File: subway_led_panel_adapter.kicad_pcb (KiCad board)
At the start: 4 copper layers, 63.5 x 63.5 mm, 28 parts, among them J1 Conn_02x06_Odd_Even, J2 Conn_02x10_Odd_Even, J3 Conn_02x06_Odd_Even, J4 Conn_02x20_Odd_Even, U1 74AHCT244, U2 ChinaBluePill, U3 74LVC1G123

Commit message: more work
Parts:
- added H1: MountingHole_Pad, MountingHole:MountingHole_3.2mm_M3_Pad, F.Cu at (124.5, 104.1)
- added H2: MountingHole_Pad, MountingHole:MountingHole_3.2mm_M3_Pad, F.Cu at (176.5, 48.3)
- added R9: 1k, Resistor_SMD:R_0603_1608Metric, F.Cu at (158.2, 86.2)
- R3: value 1k -> 100k
- moved J3 0.76 mm to (150.9, 61.0)
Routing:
- net /PB15: track 25.7 -> 40.2 mm, vias 0 -> 1
- net /PB14: track 30.0 -> 43.3 mm, vias 1 -> 0
- net /ROW_~{E1}: track 91.4 -> 80.2 mm, vias 2 -> 3
- net /~{OE}/SW/~{ED}_inv_LV: track 64.1 -> 56.9 mm, vias 2 -> 1
- net /LE/MOD/CA_LV: track 28.8 -> 35.9 mm
- net /PA9: track 39.7 -> 46.6 mm
- net /PB3: track 43.2 -> 47.3 mm
- net /ROW_A2: track 13.9 -> 11.2 mm, vias 0 -> 1
- net +3V3: track 88.9 -> 86.4 mm, vias 0 -> 1
- net /PB1: track 10.5 -> 12.8 mm
- net /PB4: track 49.8 -> 52.1 mm
- net /COPI_LV: track 35.4 -> 33.2 mm, vias 2 -> 1
- net /PB11: track 10.8 -> 8.64 mm
- net GND: track 18.8 -> 21.0 mm
- net /PB12: track 33.3 -> 35.2 mm
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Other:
- board size 63.5 x 63.5 mm -> 59.7 x 63.5 mm
- board text added: "Default Shiftregister Chain: COPI - Reg A - ... ... - Reg C - Reg B - CIPO"
- board text removed: "Default Shiftregister Chain: COPI - Reg A - Reg C - Reg B - CIPO"

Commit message: general cleanup
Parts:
- moved D4 2.69 mm to (166.4, 47.0)
- moved R8 2.69 mm to (166.4, 50.9)
- moved D1 2.54 mm to (164.0, 47.0)
- moved R5 2.54 mm to (164.0, 50.9)
- moved D2 2.43 mm to (161.5, 47.0)
- moved R6 2.43 mm to (161.5, 50.9)
- moved C1 2.17 mm to (157.2, 91.1)
- moved D3 2.14 mm to (168.7, 47.0)
- moved R7 2.14 mm to (168.7, 50.9)
- moved R1 1.78 mm to (166.9, 64.8)
- moved R2 1.78 mm to (166.9, 66.5)
- moved R9 1.14 mm to (157.2, 86.7), turned to -90 degrees
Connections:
- J1 pad 10: GND -> /PA15
- J3 pad 10: GND -> /PA10
- U2 pad PA10: (no net) -> /PA10
- U2 pad PA15: (no net) -> /PA15
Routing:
- net /PA15: track 0.00 -> 58.0 mm
- net /PA10: track 0.00 -> 51.8 mm
- net /ROW_E2: track 80.6 -> 83.5 mm
- net /CIPO_5V: track 5.01 -> 2.57 mm
- net +5V: track 19.0 -> 16.9 mm
- net /ROW_~{E1}: track 80.2 -> 78.2 mm
- net GND: track 21.0 -> 19.1 mm
- net /LE/MOD/CA_LV: track 35.9 -> 34.9 mm
- net /PB12: track 35.2 -> 34.3 mm
- net /PB13: track 33.4 -> 32.5 mm
- net /PB14: track 43.3 -> 42.6 mm
- net /PB15: track 40.2 -> 39.6 mm
- net /PB10: track 13.7 -> 13.1 mm
- net /PB1: track 12.8 -> 12.3 mm, vias 0 -> 1
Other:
- board text added: "3v3 5V E2 ~{E1}"
- board text removed: "5V 3v3 ~{E1} E2"

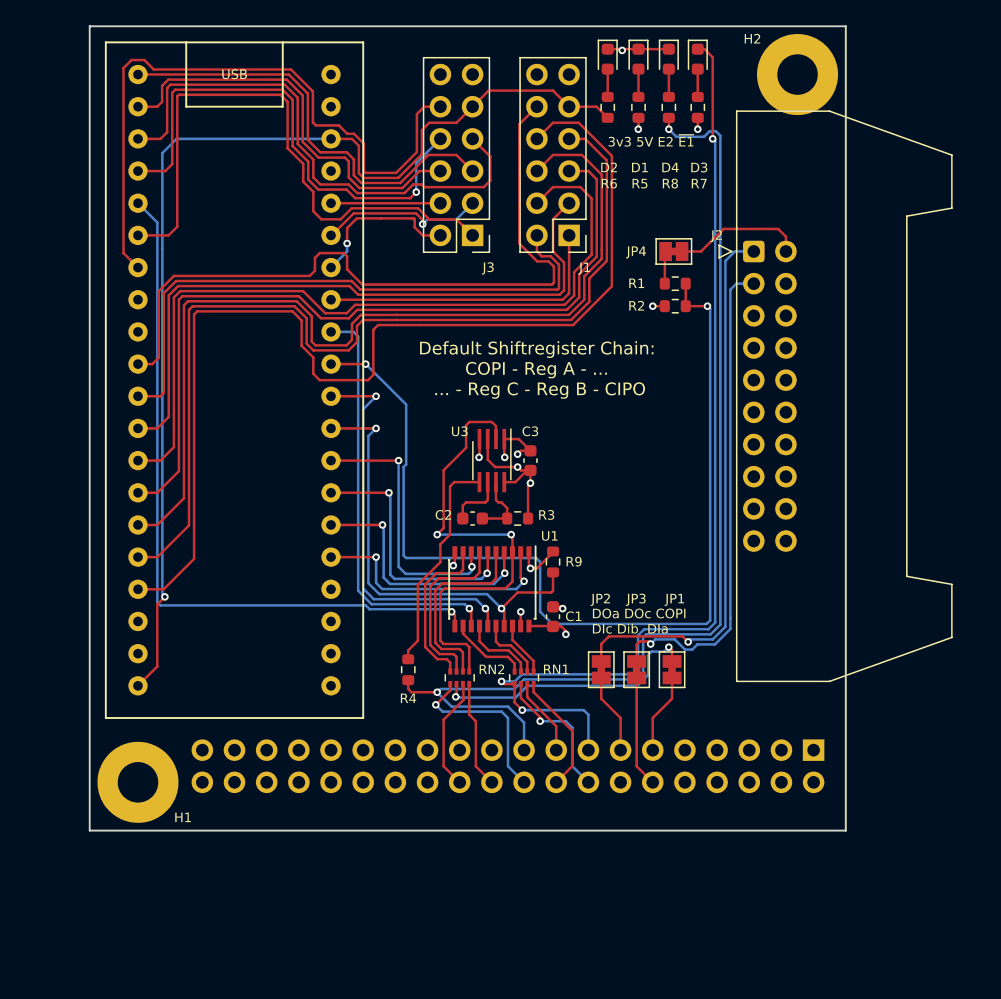
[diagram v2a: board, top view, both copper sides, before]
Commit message: Add "pmpd" style connector for 3v3 signals, rearrange, add mounting holes.
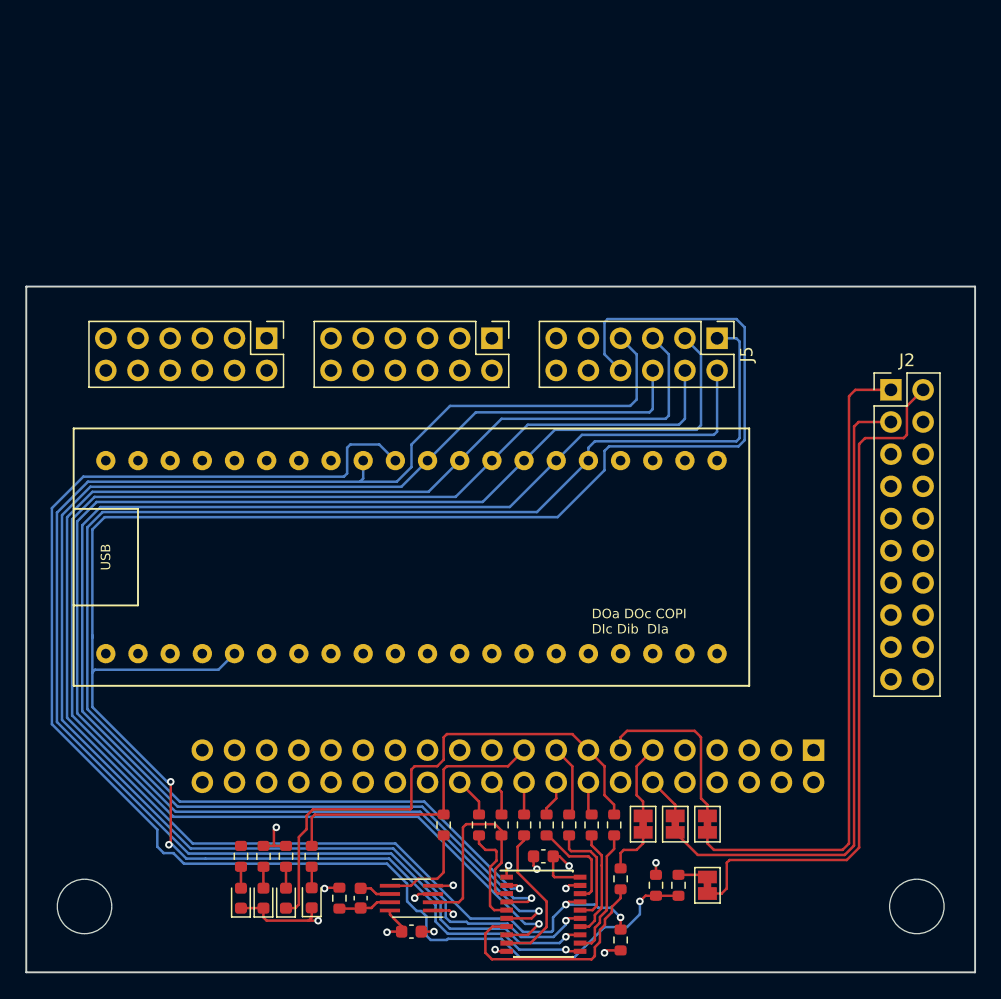
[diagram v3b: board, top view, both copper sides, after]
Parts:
- removed H1, H2: MountingHole_Pad, MountingHole:MountingHole_3.2mm_M3_Pad
- removed RN1, RN2: 68R, Resistor_SMD:R_Array_Concave_4x0402
- added H3: MountingHole, MountingHole:MountingHole_4.3mm_M4, F.Cu at (120.2, 113.9)
- added H4: MountingHole, MountingHole:MountingHole_4.3mm_M4, F.Cu at (185.9, 113.9)
- added J5: Conn_02x06_Odd_Even, Connector_PinHeader_2.54mm:PinHeader_2x06_P2.54mm_Vertical, F.Cu at (170.2, 69.1)
- added R10: 68R, Resistor_SMD:R_0603_1608Metric, F.Cu at (156.7, 107.5)
- added R11: 68R, Resistor_SMD:R_0603_1608Metric, F.Cu at (158.5, 107.5)
- added R12: 68R, Resistor_SMD:R_0603_1608Metric, F.Cu at (160.3, 107.5)
- added R13: 68R, Resistor_SMD:R_0603_1608Metric, F.Cu at (162.1, 107.5)
- added R14: 68R, Resistor_SMD:R_0603_1608Metric, F.Cu at (153.2, 107.5)
- added R15: 68R, Resistor_SMD:R_0603_1608Metric, F.Cu at (151.4, 107.5)
- added R16: 68R, Resistor_SMD:R_0603_1608Metric, F.Cu at (162.6, 111.8)
- added R17: 68R, Resistor_SMD:R_0603_1608Metric, F.Cu at (154.9, 107.5)
- J2: footprint Connector_IDC:IDC-Header_2x10_P2.54mm_Latch_Horizontal -> Connector_PinHeader_2.54mm:PinHeader_2x10_P2.54mm_Vertical
- moved D3 73.8 mm to (136.1, 113.3), turned to 90 degrees
- moved D1 72.6 mm to (134.4, 113.3), turned to 90 degrees
- moved D2 72.3 mm to (132.6, 113.3), turned to 90 degrees
- moved D4 72.0 mm to (138.2, 113.3), turned to 90 degrees
- moved R7 67.5 mm to (136.1, 110.0), turned to 90 degrees
- moved R5 66.1 mm to (134.4, 110.0), turned to 90 degrees
- moved R6 65.8 mm to (132.6, 110.0), turned to 90 degrees
- moved R8 65.5 mm to (138.2, 110.0), turned to 90 degrees
- moved JP4 50.1 mm to (169.4, 112.3), turned to 90 degrees
- moved R1 47.5 mm to (167.1, 112.3), turned to -90 degrees
- moved U2 45.8 mm to (170.2, 94.0), turned to 90 degrees
- moved R2 45.7 mm to (165.4, 112.3), turned to -90 degrees
- moved C3 38.4 mm to (146.1, 115.9), turned to 180 degrees
- moved U3 35.1 mm to (146.1, 113.3), turned to 180 degrees
- moved R3 33.1 mm to (140.4, 113.3), turned to 90 degrees
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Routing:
- net /ROW_A2_LV: track 20.7 -> 120.7 mm, vias 2 -> 1
- net /ROW_A0_LV: track 20.1 -> 120.0 mm, vias 2 -> 1
- net /~{OE}/SW/~{ED}_inv_LV: track 56.9 -> 156.4 mm, vias 1 -> 3
- net /ROW_A1_LV: track 20.0 -> 116.4 mm, vias 2 -> 1
- net /ROW_~{E1}_LV: track 21.3 -> 117.6 mm, vias 2 -> 1
- net /LE/MOD/CA_LV: track 34.9 -> 128.1 mm
- net /COPI_LV: track 33.2 -> 123.7 mm
- net /CLK_LV: track 30.9 -> 118.9 mm, vias 2 -> 1
- net +3V3: track 86.1 -> 0.00 mm, vias 1 -> 0
- net /PB9: track 85.0 -> 0.00 mm
- net /PB8: track 74.2 -> 0.00 mm
- net /PB7: track 73.1 -> 0.00 mm
- net /PB6: track 62.9 -> 0.00 mm
- net /PB5: track 61.6 -> 0.00 mm
- net /ROW_E2: track 83.5 -> 23.3 mm, vias 2 -> 0
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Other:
- board size 59.7 x 63.5 mm -> 74.9 x 54.1 mm
- board text removed: "3v3 5V E2 ~{E1}"
- board text removed: "Default Shiftregister Chain: COPI - Reg A - ... ... - Reg C - Reg B - CIPO"

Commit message: further work
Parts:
- added C4: 100n, Capacitor_SMD:C_0603_1608Metric, F.Cu at (143.3, 107.8)
- added D5: LED, LED_SMD:LED_0603_1608Metric, F.Cu at (124.2, 103.1)
- added D6: LED, LED_SMD:LED_0603_1608Metric, F.Cu at (122.4, 103.1)
- added D7: LED, LED_SMD:LED_0603_1608Metric, F.Cu at (120.7, 103.1)
- added D8: LED, LED_SMD:LED_0603_1608Metric, F.Cu at (118.9, 103.1)
- added JP5: SolderJumper_2_Bridged, Jumper:SolderJumper-2_P1.3mm_Bridged_Pad1.0x1.5mm, B.Cu at (172.7, 98.4)
- added JP6: SolderJumper_2_Bridged, Jumper:SolderJumper-2_P1.3mm_Bridged_Pad1.0x1.5mm, B.Cu at (134.6, 98.4)
- added R18: 1k, Resistor_SMD:R_0603_1608Metric, F.Cu at (124.2, 99.8)
- added R19: 1k, Resistor_SMD:R_0603_1608Metric, F.Cu at (122.4, 99.8)
- added R20: 1k, Resistor_SMD:R_0603_1608Metric, F.Cu at (120.7, 99.8)
- added R21: 1k, Resistor_SMD:R_0603_1608Metric, F.Cu at (118.9, 99.8)
- added R22: 68R, Resistor_SMD:R_0603_1608Metric, F.Cu at (146.6, 107.4)
- added U4: 74LVC1GU04DRL, Package_TO_SOT_SMD:SOT-553, F.Cu at (143.4, 109.9)
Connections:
- D4 pad 1: GND -> /ROW_~{E2}
- J4 pad 1: GND -> Net-(J4-Pad1)
- J4 pad 10: GND -> Net-(J4-Pad1)
- J4 pad 19: /ROW_E2 -> /ROW_~{E2}
- J4 pad 2: GND -> Net-(J4-Pad1)
- J4 pad 3: GND -> Net-(J4-Pad1)
- J4 pad 31: +5V -> Net-(J4-Pad31)
- J4 pad 32: +5V -> Net-(J4-Pad31)
- J4 pad 33: +5V -> Net-(J4-Pad31)
- J4 pad 34: +5V -> Net-(J4-Pad31)
- J4 pad 35: +5V -> Net-(J4-Pad31)
- J4 pad 36: +5V -> Net-(J4-Pad31)
- J4 pad 37: +5V -> Net-(J4-Pad31)
- J4 pad 38: +5V -> Net-(J4-Pad31)
- J4 pad 39: +5V -> Net-(J4-Pad31)
- J4 pad 4: GND -> Net-(J4-Pad1)
- J4 pad 40: +5V -> Net-(J4-Pad31)
- J4 pad 5: GND -> Net-(J4-Pad1)
- J4 pad 6: GND -> Net-(J4-Pad1)
- J4 pad 7: GND -> Net-(J4-Pad1)
- J4 pad 8: GND -> Net-(J4-Pad1)
- J4 pad 9: GND -> Net-(J4-Pad1)
- J5 pad 11: unconnected-(J5-Pad11) -> (no net)
- J5 pad 12: unconnected-(J5-Pad12) -> (no net)
- R4 pad 1: /ROW_E2 -> /ROW_~{E2}
- R8 pad 2: /ROW_E2 -> +5V
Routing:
- net +3V3: track 0.00 -> 125.5 mm, vias 0 -> 2
- net /PB4: track 0.00 -> 81.8 mm
- net /PA15: track 0.00 -> 81.3 mm
- net /PB3: track 0.00 -> 81.1 mm
- net /PB6: track 0.00 -> 76.1 mm
- net /PB5: track 0.00 -> 75.8 mm
- net /PB8: track 0.00 -> 70.0 mm
- net /PB7: track 0.00 -> 69.8 mm
- net /PB9: track 0.00 -> 62.7 mm
- net /PB13: track 0.00 -> 52.5 mm
- net /PB12: track 0.00 -> 49.3 mm
- net /PA9: track 0.00 -> 46.9 mm
- net /PB15: track 0.00 -> 39.4 mm
- net /PB14: track 0.00 -> 39.3 mm
- net /PA10: track 0.00 -> 38.3 mm, vias 0 -> 1
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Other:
- board text added: "- ⏚ DO LE A2 A0 - ⏚ OE CLK E1 A1"
- board text added: "3V 5V E1 E2"
- board text added: "5V"
- board text added: "B12 B13 B14 B15"
- board text added: "CLK LE OE A0 A1 A2 ~{E1}"
- board text added: "CPIO DOb"
- board text added: "DIa DIb DIc COPI DOc DOa"
- board text added: "GND"
- board text added: "https://github.com/vogelchr/subway_led_panel_adapter"
- board text added: "~{E2}"
- board text added: "↓ last panel ↓"
- board text added: "⏚ 3V3 B14 B12 B10 A9 ⏚ A10 B15 B13 B11 B1"
- board text added: "⏚ 3V3 B8 B6 B4 B0 ⏚ A15 B9 B7 B5 B3"
- board text removed: "DOa DOc COPI DIc Dib DIa"

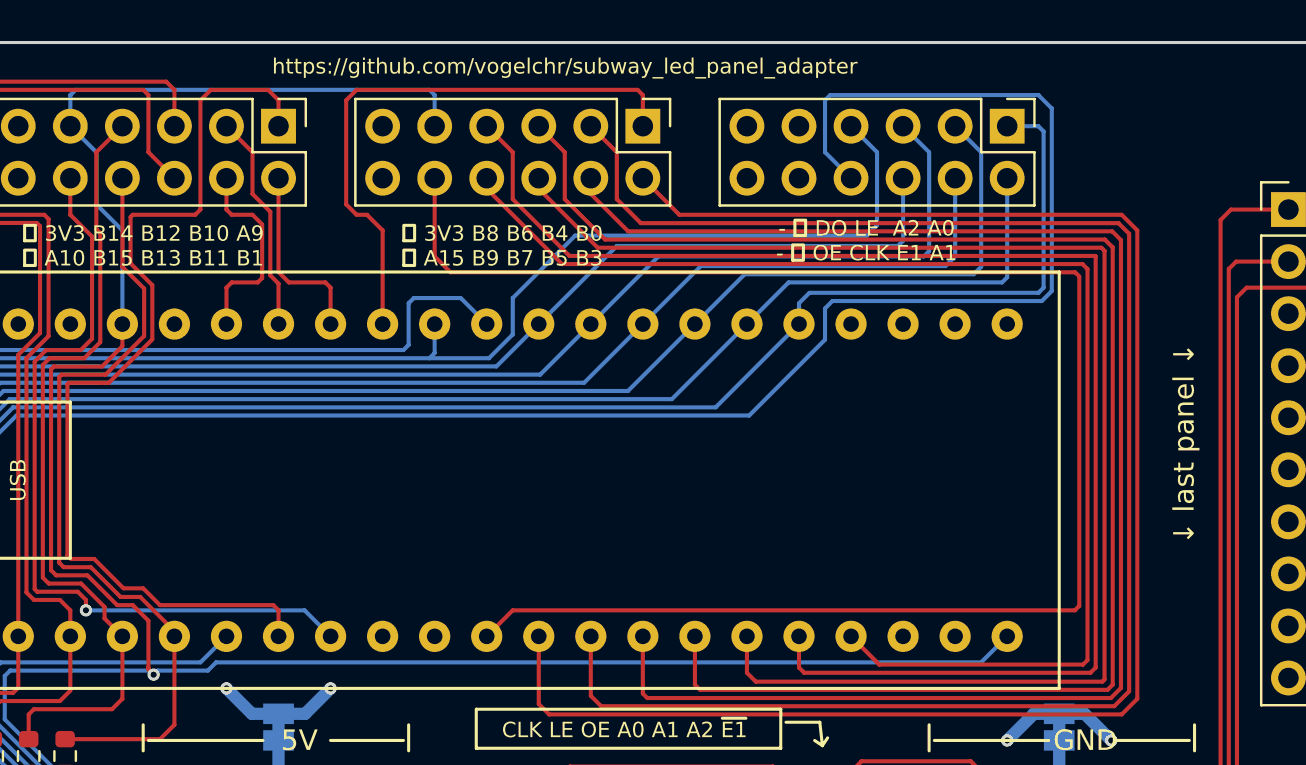
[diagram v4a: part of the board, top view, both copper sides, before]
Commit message: Start working on Rev. B: Adds 3v3 Regulator
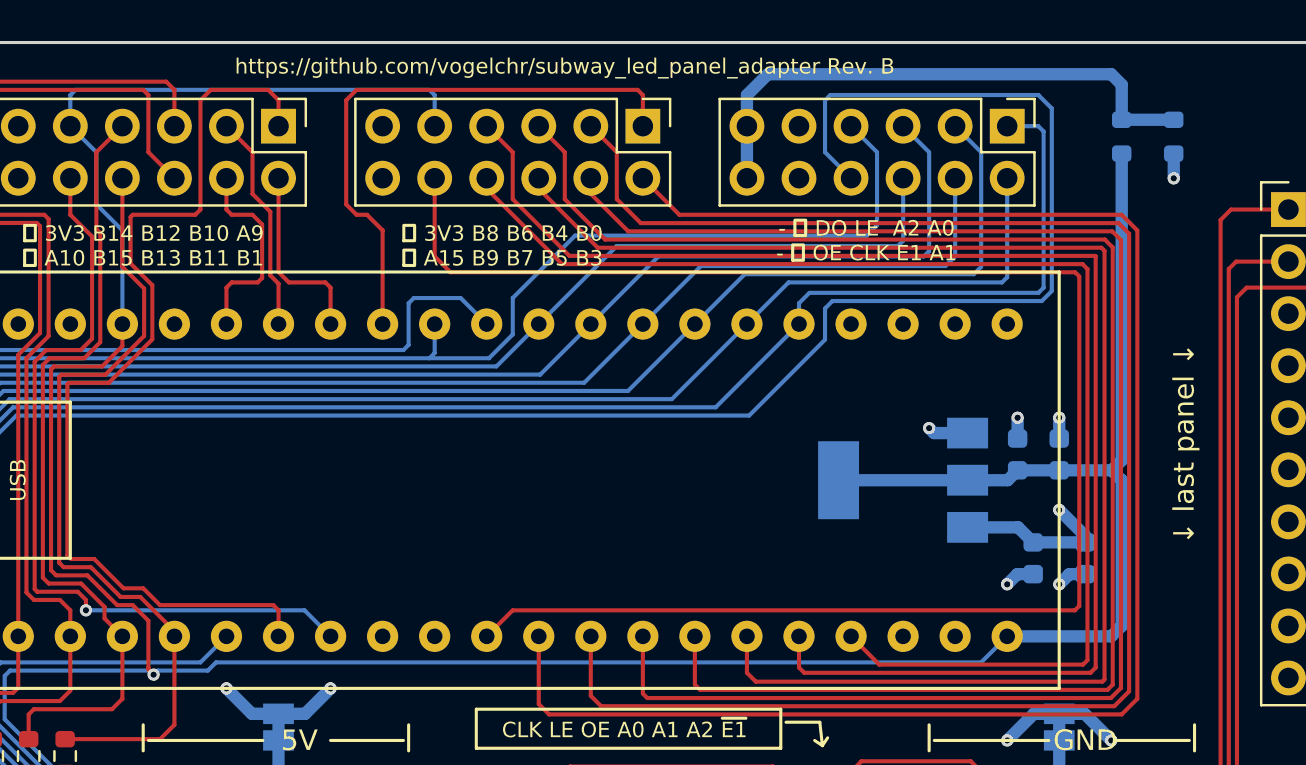
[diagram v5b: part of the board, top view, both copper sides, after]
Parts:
- added C5: 100n, Capacitor_SMD:C_0603_1608Metric, B.Cu at (171.4, 90.2)
- added C6: 10u, Capacitor_SMD:C_0603_1608Metric, B.Cu at (174.0, 90.2)
- added C7: 100n, Capacitor_SMD:C_0603_1608Metric, B.Cu at (170.7, 85.1)
- added C8: 10u, Capacitor_SMD:C_0603_1608Metric, B.Cu at (172.7, 85.1)
- added R23: DNP, Resistor_SMD:R_0603_1608Metric, B.Cu at (178.3, 69.6)
- added R24: 0R, Resistor_SMD:R_0603_1608Metric, B.Cu at (175.8, 69.6)
- added U5: AMS1117-3.3, Package_TO_SOT_SMD:SOT-223-3_TabPin2, B.Cu at (165.1, 86.4)
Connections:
- J2 pad 10: (no net) -> unconnected-(J2-Pin_10)
- J2 pad 12: (no net) -> unconnected-(J2-Pin_12)
- J2 pad 14: (no net) -> unconnected-(J2-Pin_14)
- J2 pad 15: (no net) -> unconnected-(J2-Pin_15)
- J2 pad 16: (no net) -> unconnected-(J2-Pin_16)
- J2 pad 17: (no net) -> unconnected-(J2-Pin_17)
- J2 pad 18: (no net) -> unconnected-(J2-Pin_18)
- J2 pad 19: (no net) -> unconnected-(J2-Pin_19)
- J2 pad 20: (no net) -> unconnected-(J2-Pin_20)
- J2 pad 4: (no net) -> unconnected-(J2-Pin_4)
- J2 pad 5: (no net) -> unconnected-(J2-Pin_5)
- J2 pad 6: (no net) -> unconnected-(J2-Pin_6)
- J2 pad 7: (no net) -> unconnected-(J2-Pin_7)
- J2 pad 8: (no net) -> unconnected-(J2-Pin_8)
- J2 pad 9: (no net) -> unconnected-(J2-Pin_9)
- J4 pad 14: (no net) -> unconnected-(J4-Pin_14)
- J4 pad 25: (no net) -> unconnected-(J4-Pin_25)
- J4 pad 26: (no net) -> unconnected-(J4-Pin_26)
- J4 pad 27: (no net) -> /DOx_A0
- J4 pad 28: (no net) -> /DOx_A1
- J4 pad 29: (no net) -> /DOx
- J4 pad 30: (no net) -> unconnected-(J4-Pin_30)
- J5 pad 11: (no net) -> Net-(J5-Pin_11)
- J5 pad 12: (no net) -> Net-(J5-Pin_11)
- U2 pad 5V: (no net) -> unconnected-(U2-Pad5V)
- U2 pad NRST: (no net) -> unconnected-(U2-PadNRST)
- U2 pad PA11: (no net) -> unconnected-(U2-PadPA11)
- U2 pad PA12: (no net) -> unconnected-(U2-PadPA12)
- U2 pad PC13: (no net) -> unconnected-(U2-PadPC13)
- U2 pad PC14: (no net) -> unconnected-(U2-PadPC14)
- U2 pad PC15: (no net) -> unconnected-(U2-PadPC15)
- U2 pad VBAT: (no net) -> unconnected-(U2-PadVBAT)
- U4 pad 1: (no net) -> unconnected-(U4-NC)
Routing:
- net +3V3: track 125.5 -> 168.3 mm
- net Net-(J5-Pin_11): track 0.00 -> 27.2 mm
- net +5V: track 25.2 -> 34.5 mm, vias 8 -> 10
- net GND: track 29.1 -> 36.0 mm, vias 15 -> 20
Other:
- board text added: "https://github.com/vogelchr/subway_led_panel_adapter Rev. B"
- board text removed: "https://github.com/vogelchr/subway_led_panel_adapter"

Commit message: Cleanup rev. B.
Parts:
- removed R4: 68R, Resistor_SMD:R_0603_1608Metric
- moved C7 5.33 mm to (176.0, 85.1)
- moved C8 5.33 mm to (178.1, 85.1)
- moved U5 5.09 mm to (170.2, 86.1)
- moved C5 4.68 mm to (176.0, 89.2)
- moved C6 4.19 mm to (178.1, 89.2)
- moved R23 2.34 mm to (176.0, 69.1), turned to 0 degrees
- moved R24 2.05 mm to (176.0, 71.6), turned to 0 degrees
- moved U4 0.89 mm to (144.3, 109.9)
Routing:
- net Net-(U3A-Q): track 13.5 -> 3.11 mm
- net +3V3: track 168.3 -> 171.9 mm
- net Net-(U1-2Y2): track 19.1 -> 21.6 mm
- net +5V: track 34.5 -> 32.1 mm
- net Net-(J5-Pin_11): track 27.2 -> 26.0 mm
- net Net-(R22-Pad2): track 4.43 -> 3.54 mm
- net Net-(U1-2Y1): track 8.24 -> 7.38 mm
- net GND: track 36.0 -> 36.8 mm
- net /ROW_~{E1}: track 42.6 -> 43.2 mm
- net /PB9: track 62.7 -> 62.2 mm
- net /PB7: track 69.8 -> 69.2 mm
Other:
- board text added: "+5V"
- board text added: "3v3 LDO, do not populate when using the BluePill module!"
- board text added: "Vcc ⏚ DO LE A2 A0 Vcc ⏚ OE CLK E1 A1"
- board text added: "Vcc: 5V 3V3"
- board text added: "↓ spare GPIO ↓"
- board text removed: "- ⏚ DO LE A2 A0 - ⏚ OE CLK E1 A1"
